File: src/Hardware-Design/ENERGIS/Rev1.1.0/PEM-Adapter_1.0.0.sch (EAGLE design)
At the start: 11 parts

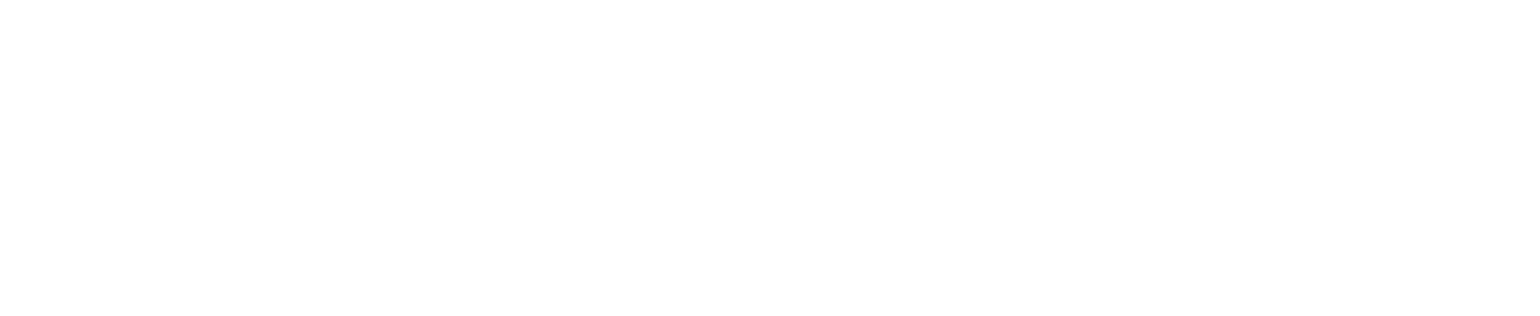
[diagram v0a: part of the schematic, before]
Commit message: clear documentation, software bugfix
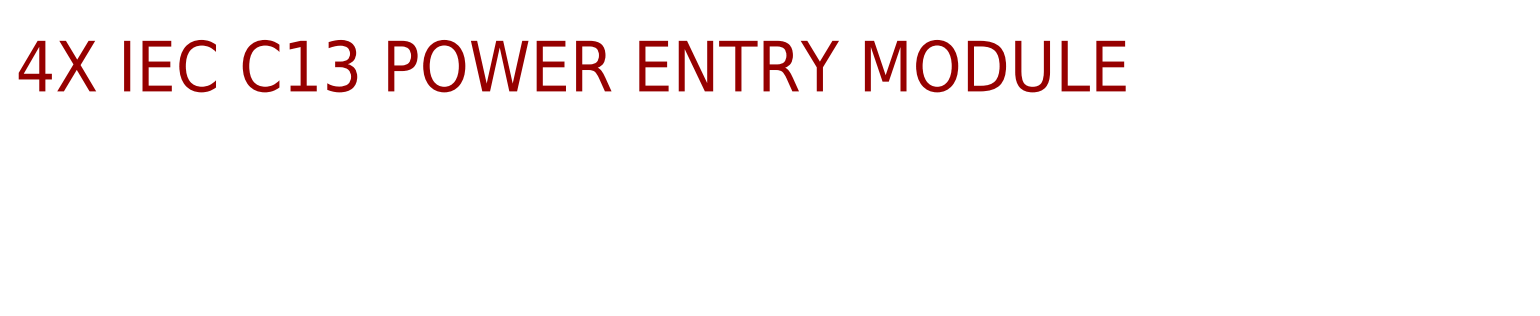
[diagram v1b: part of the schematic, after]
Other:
- note added: "4X IEC C13 POWER ENTRY MODULE"
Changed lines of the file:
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@@
 <text x="264.16" y="40.64" size="6.4516" layer="94">PEM-Adapter Board</text>
 <text x="261.62" y="27.94" size="3.81" layer="94">PEM-Adapter</text>
+<text x="10.16" y="241.3" size="6.4516" layer="94">4X IEC C13 POWER ENTRY MODULE</text>
 </plain>
 <instances>
